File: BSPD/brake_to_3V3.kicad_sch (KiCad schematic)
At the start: 6 parts

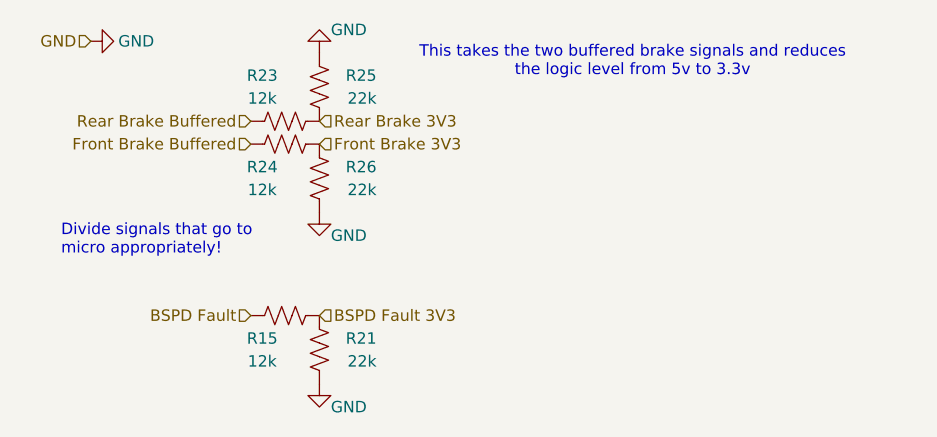
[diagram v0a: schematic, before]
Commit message: Overhaul of BPSD to V3.0
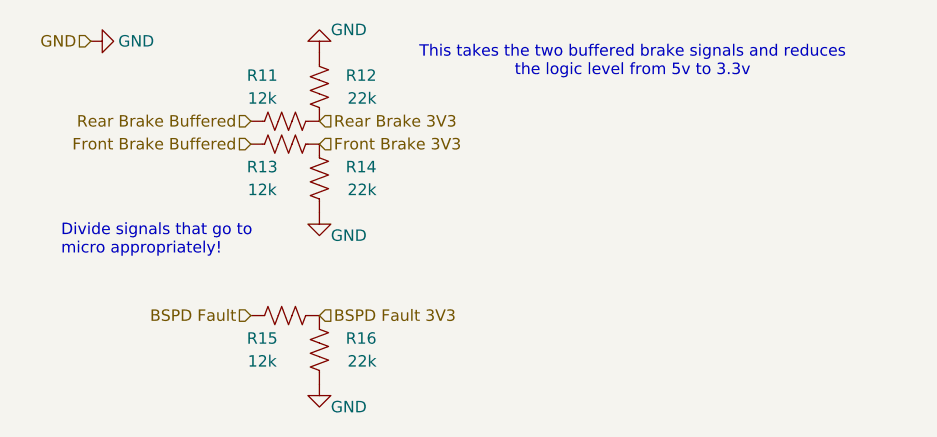
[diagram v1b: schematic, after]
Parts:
- renumbered R23 to R11, R25 to R12, R24 to R13, R26 to R14, R21 to R16
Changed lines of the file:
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@@
 		(on_board yes)
 		(dnp no)
-		(property "Reference" "R25"
+		(property "Reference" "R12"
 			(at 50.8 20.32 0)
 			(effects
@@
 			(project "BSPD"
 				(path "/9b958334-fa88-4811-8197-71444a07b1b5/5896a7f2-04c2-4c50-b54b-d702debc4319"
-					(reference "R25")
+					(reference "R12")
 					(unit 1)
 				)
@@
 		(on_board yes)
 		(dnp no)
-		(property "Reference" "R23"
+		(property "Reference" "R11"
 			(at 38.1 20.32 90)
 			(effects
@@
 			(project "BSPD"
 				(path "/9b958334-fa88-4811-8197-71444a07b1b5/5896a7f2-04c2-4c50-b54b-d702debc4319"
-					(reference "R23")
+					(reference "R11")
 					(unit 1)
 				)
@@
 		(on_board yes)
 		(dnp no)
-		(property "Reference" "R26"
+		(property "Reference" "R14"
 			(at 50.8 30.48 0)
 			(effects
@@
 			(project "BSPD"
 				(path "/9b958334-fa88-4811-8197-71444a07b1b5/5896a7f2-04c2-4c50-b54b-d702debc4319"
-					(reference "R26")
+					(reference "R14")
 					(unit 1)
 				)
@@
 		(on_board yes)
 		(dnp no)
-		(property "Reference" "R21"
+		(property "Reference" "R16"
 			(at 50.8 49.53 0)
 			(effects
@@
 			(project "BSPD"
 				(path "/9b958334-fa88-4811-8197-71444a07b1b5/5896a7f2-04c2-4c50-b54b-d702debc4319"
-					(reference "R21")
+					(reference "R16")
 					(unit 1)
 				)
@@
 		(on_board yes)
 		(dnp no)
-		(property "Reference" "R24"
+		(property "Reference" "R13"
 			(at 38.1 30.48 90)
 			(effects
@@
 			(project "BSPD"
 				(path "/9b958334-fa88-4811-8197-71444a07b1b5/5896a7f2-04c2-4c50-b54b-d702debc4319"
-					(reference "R24")
-					(unit 1)
-				)
+					(reference "R13")
+					(unit 1)
+				)
